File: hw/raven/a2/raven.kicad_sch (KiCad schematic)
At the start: 76 parts, among them J101 Pinhdr_01x02, J103 JTAG IN, J106 Pinhdr_01x02, J203 Pinhdr_01x03, SW2 SW_Push, U101 74LS148, U102 74AHC157, U103 SN74LVCH16245, U105 CY2308, U106 SN74LVCH16245, U108 ATF1508, U2 MC68060, U4 MC68150, X101 48Mhz (3.3V)

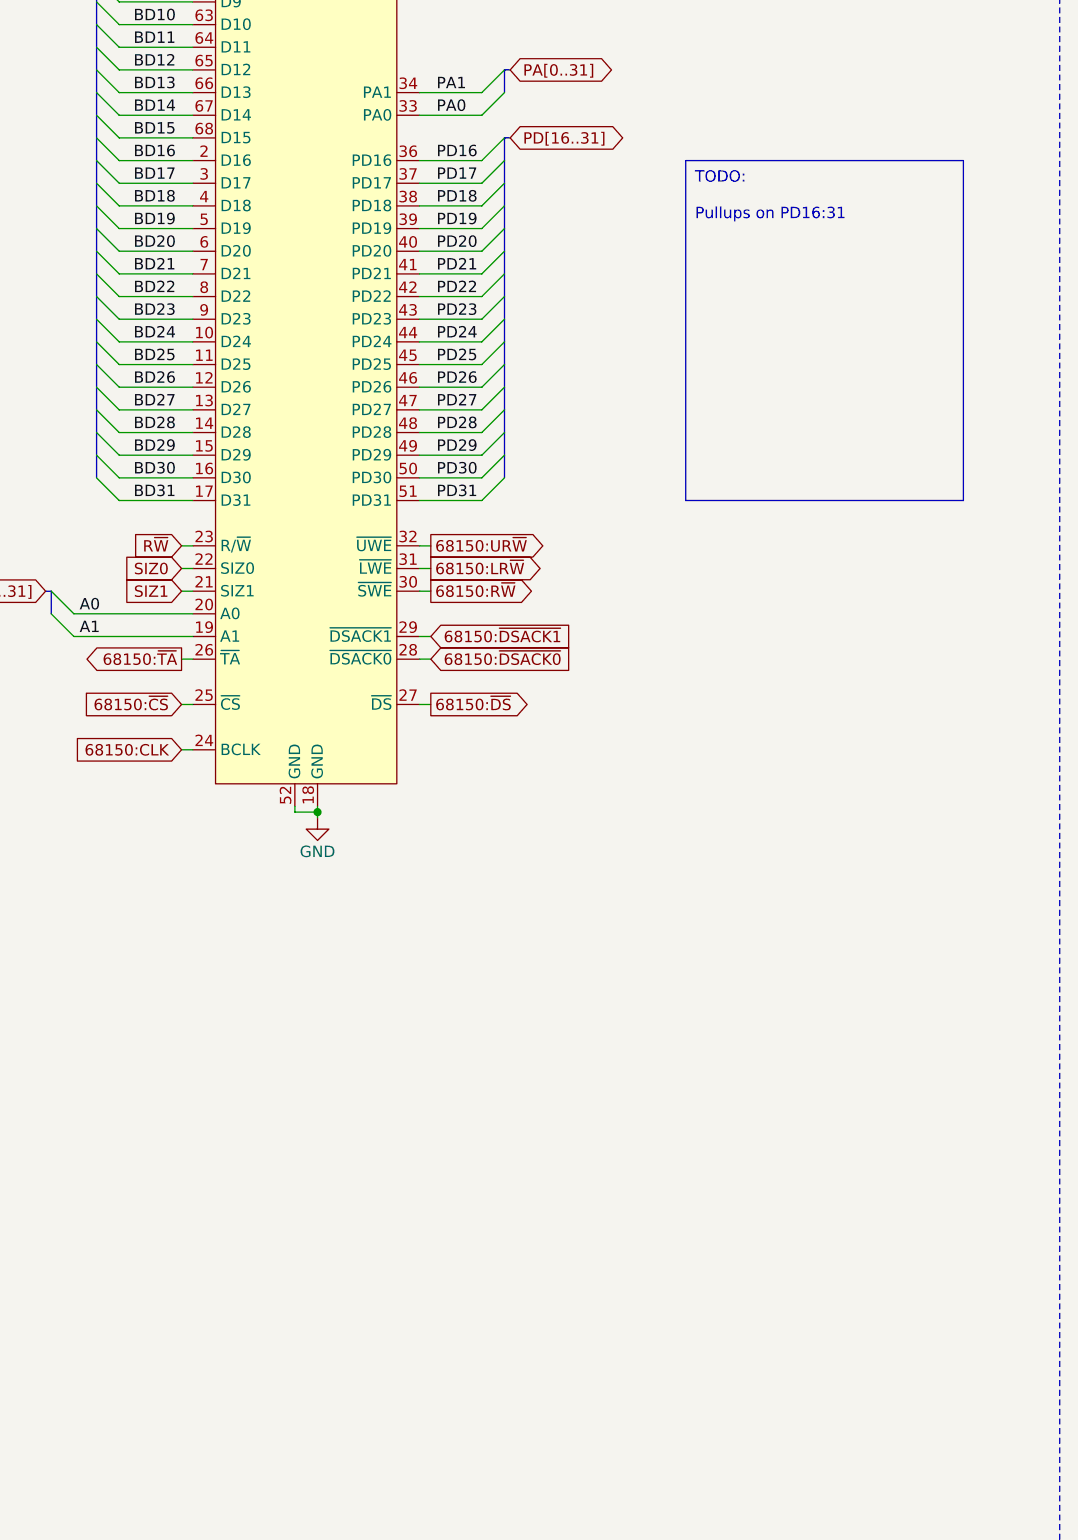
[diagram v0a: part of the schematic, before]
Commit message: Raven.A2: pullups on MC68150 databus
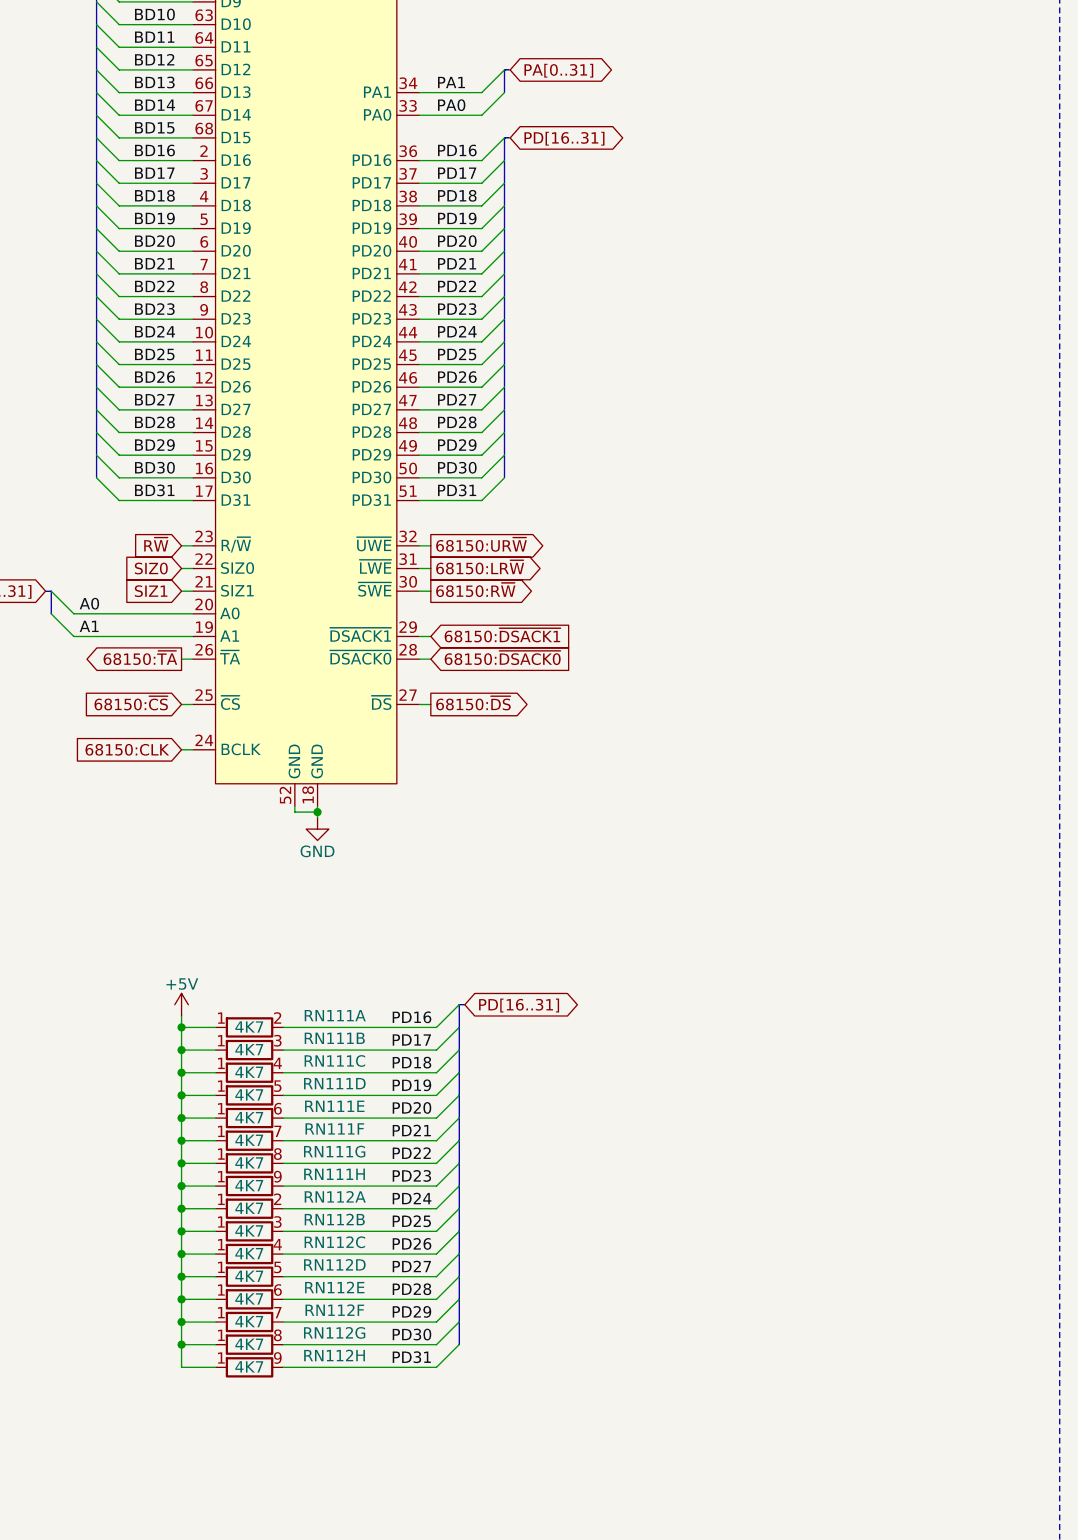
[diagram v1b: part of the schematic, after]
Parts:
- added RN111, RN112: 4K7, Resistor_THT:R_Array_SIP9, symbol Device:R_Network08_Split
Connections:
- net +5V: now also RN111.1 (R1), RN111.1 (R1), RN111.1 (R1), RN111.1 (R1), RN111.1 (R1), RN111.1 (R1), RN111.1 (R1), RN111.1 (R1), RN112.1 (R1), RN112.1 (R1), RN112.1 (R1), RN112.1 (R1), RN112.1 (R1), RN112.1 (R1), RN112.1 (R1), RN112.1 (R1)
- net PD16: now also RN111.2 (R1.2)
- net PD17: now also RN111.3 (R2.2)
- net PD18: now also RN111.4 (R3.2)
- net PD19: now also RN111.5 (R4.2)
- net PD20: now also RN111.6 (R5.2)
- net PD21: now also RN111.7 (R6.2)
- net PD22: now also RN111.8 (R7.2)
- net PD23: now also RN111.9 (R8.2)
- net PD24: now also RN112.2 (R1.2)
- net PD25: now also RN112.3 (R2.2)
- net PD26: now also RN112.4 (R3.2)
- net PD27: now also RN112.5 (R4.2)
- net PD28: now also RN112.6 (R5.2)
- net PD29: now also RN112.7 (R6.2)
- net PD30: now also RN112.8 (R7.2)
- net PD31: now also RN112.9 (R8.2)

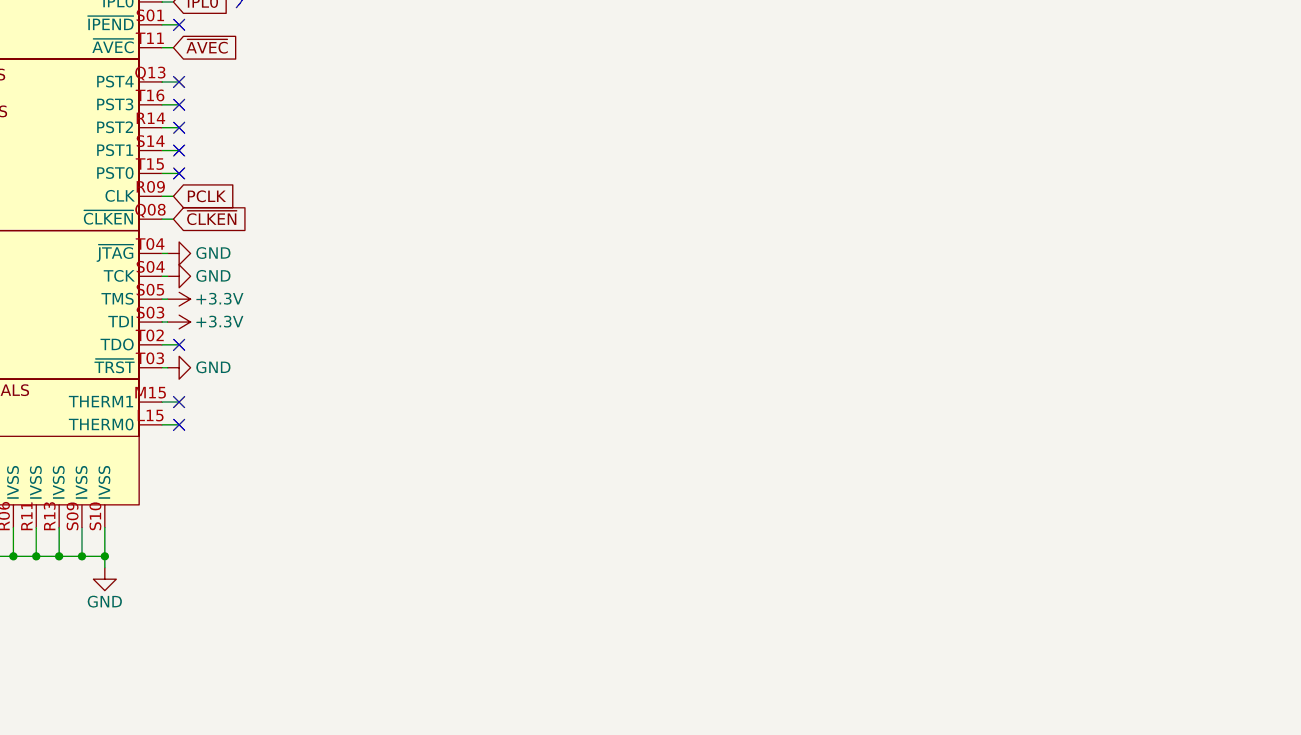
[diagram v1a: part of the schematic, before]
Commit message: rev.A2 updates
Added i2c DAC for reading cpu core temperature
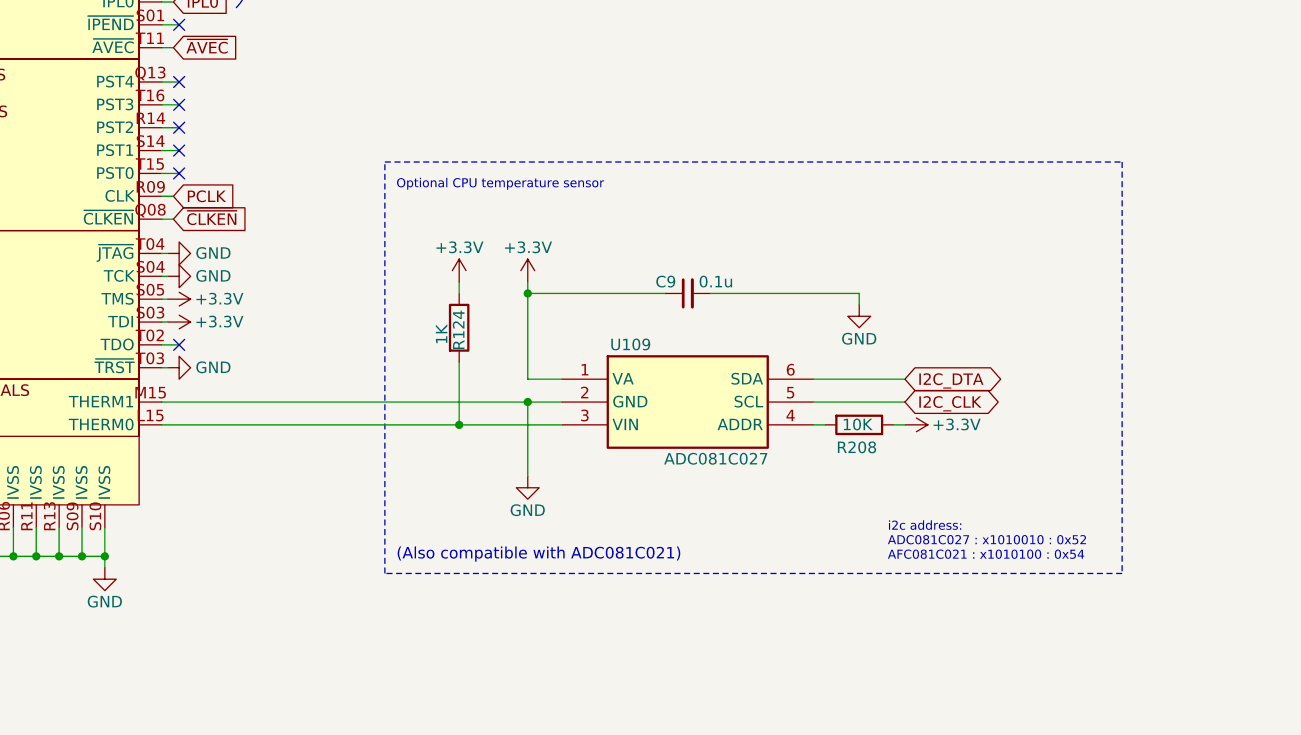
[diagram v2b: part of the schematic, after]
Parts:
- added C9: 0.1u, Capacitor_SMD:C_1206_3216Metric_Pad1.33x1.80mm_HandSolder, symbol 68k:c_100nf_smd1206
- added R124: 1K, Resistor_SMD:R_1206_3216Metric_Pad1.30x1.75mm_HandSolder, symbol Device:R
- added R208: 10K, Resistor_SMD:R_1206_3216Metric_Pad1.30x1.75mm_HandSolder, symbol Device:R
- added U109: ADC081C027, SOT95P280X110-6N, symbol 68k:ADC081C027CIMKX_NOPB
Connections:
- net +3.3V: now also C9.1, R124.1, R208.1, U109.1 (VA)
- net GND: now also U2.M15 (THERM1), C9.2, U109.2 (GND)
- net at U2.L15 (THERM0): now also R124.2, U109.3 (VIN)
- new net: R208.2, U109.4 (ADDR)
- new net I2C_CLK: U109.5 (SCL)
- new net I2C_DTA: U109.6 (SDA)
- no-connect marks 34 -> 32
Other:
- note added: "(Also compatible with ADC081C021)"
- note added: "Optional CPU temperature sensor"
- note added: "i2c address: ADC081C027 : x1010010 : 0x52 AFC081C021 : x1010100 : 0x54"

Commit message: Raven.A2 wip
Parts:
- removed C9: 0.1u, Capacitor_SMD:C_1206_3216Metric_Pad1.33x1.80mm_HandSolder, symbol 68k:c_100nf_smd1206
- removed J106: Pinhdr_01x02, Connector_PinHeader_2.54mm:PinHeader_1x02_P2.54mm_Vertical, symbol Connector_Generic:Conn_01x02
- removed R208: 10K, Resistor_SMD:R_1206_3216Metric_Pad1.30x1.75mm_HandSolder, symbol Device:R
- removed U109: ADC081C027, SOT95P280X110-6N, symbol 68k:ADC081C027CIMKX_NOPB
- renumbered C9 to C103, C10 to C104, C9 to C105, C9 to C106, C9 to C107, C514 to C108, C9 to C109, J203 to J102, J203 to J104, J203 to J105, SW2 to SW101, U4 to U104, U2 to U107
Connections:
- net PD17: now also RN112.2 (R1.2); no longer RN111.3 (R2.2)
- net PD18: now also RN111.3 (R2.2); no longer RN111.4 (R3.2)
- net PD19: now also RN112.3 (R2.2); no longer RN111.5 (R4.2)
- net PD20: now also RN111.4 (R3.2); no longer RN111.6 (R5.2)
- net PD21: now also RN112.4 (R3.2); no longer RN111.7 (R6.2)
- net PD22: now also RN111.5 (R4.2); no longer RN111.8 (R7.2)
- net PD23: now also RN112.5 (R4.2); no longer RN111.9 (R8.2)
- net PD24: now also RN111.6 (R5.2); no longer RN112.2 (R1.2)
- net PD25: now also RN112.6 (R5.2); no longer RN112.3 (R2.2)
- net PD26: now also RN111.7 (R6.2); no longer RN112.4 (R3.2)
- net PD27: now also RN112.7 (R6.2); no longer RN112.5 (R4.2)
- net PD28: now also RN111.8 (R7.2); no longer RN112.6 (R5.2)
- net PD29: now also RN112.8 (R7.2); no longer RN112.7 (R6.2)
- net PD30: now also RN111.9 (R8.2); no longer RN112.8 (R7.2)
- net ~{IRQ_MFP}: now also U101.2 (I5); no longer U101.3 (I6)
- net ~{IRQ_UART}: now also U101.3 (I6); no longer U101.2 (I5)
- net ~{ETH_CS}: now reaches U108.81 (GCLK3/IOH)
- net TEMP2: now reaches R124.2, U107.L15 (THERM0)
- no-connect marks 32 -> 33
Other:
- note added: "conflicting information"
- note added: "todo buffer cs"
- note removed: "(Also compatible with ADC081C021)"
- note removed: "Optional CPU temperature sensor"
- note removed: "i2c address: ADC081C027 : x1010010 : 0x52 AFC081C021 : x1010100 : 0x54"
- moved on the sheet: R124, RN111B, RN111C, RN111D, RN111E, RN111F, RN111G, RN111H, RN112A, RN112B, RN112C, RN112D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

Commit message: 68150:BUSCS signal separate from 68150:CS
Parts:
- removed R116: 1K, Resistor_SMD:R_1206_3216Metric_Pad1.30x1.75mm_HandSolder, symbol Device:R
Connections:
- net 68150:~{CS}: now also RN103.9 (R8.2); no longer U103.25 (~{OE2}), U103.48 (~{OE1}), U106.25 (~{OE2}), U106.48 (~{OE1})
- net 68150:~{BUSCS}: now reaches RN103.8 (R7.2)
- net 68150:~{BUSCS}: now also U103.25 (~{OE2}), U103.48 (~{OE1}), U106.25 (~{OE2}), U106.48 (~{OE1}), U108.73 (IOH)
- no-connect marks 33 -> 30
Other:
- note removed: "todo buffer cs"
- moved on the sheet: RN101A, RN101B, RN101C, RN101D, RN101E, RN101F, RN101G, RN101H, RN102D, RN102E, RN103D, RN103E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

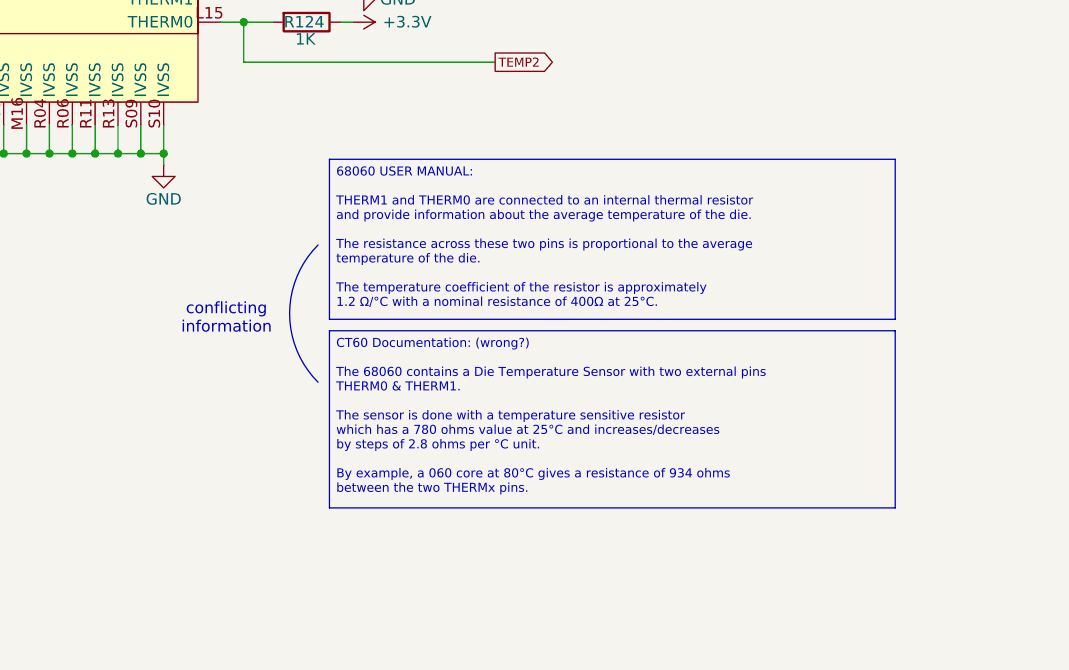
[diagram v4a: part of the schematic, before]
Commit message: A2 fan pwm+argb
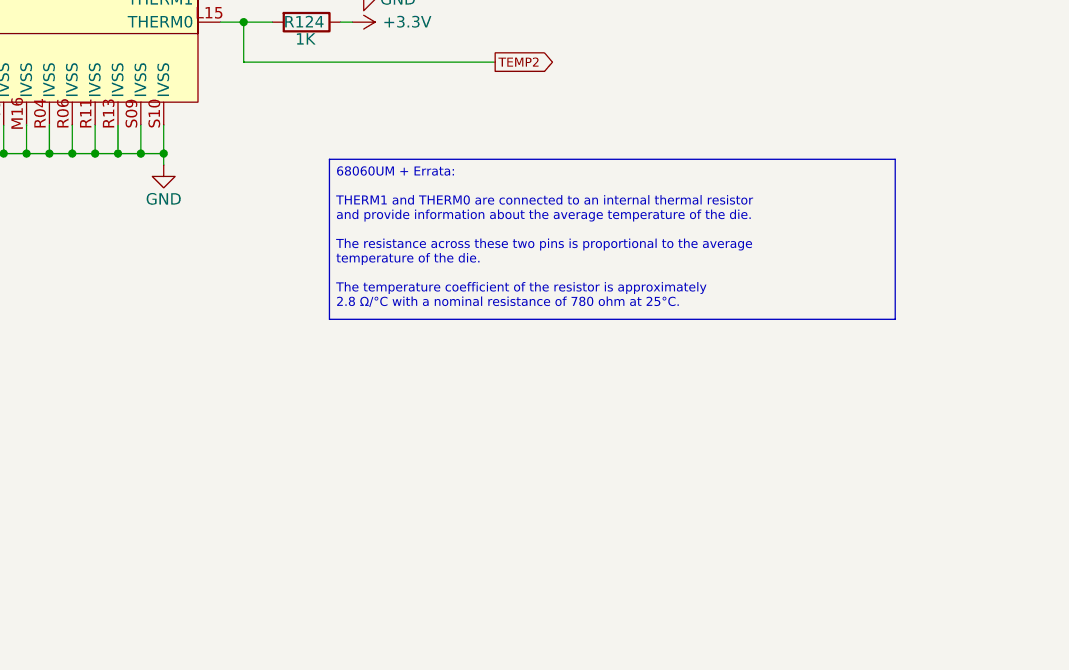
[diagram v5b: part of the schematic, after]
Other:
- note removed: "conflicting information"
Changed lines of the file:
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@@
-		)
-	)
-	(arc
-		(start 351.79 444.5)
-		(mid 348.6337 436.88)
-		(end 351.79 429.26)
-		(stroke
-			(width 0)
-			(type default)
-		)
-		(fill
-			(type none)
 		)
 	)
@@
 		)
 	)
-	(text "conflicting\ninformation"
-		(exclude_from_sim no)
-		(at 341.63 437.515 0)
-		(effects
-			(font
-				(size 1.27 1.27)
-			)
-		)
-	)
 	(text "Clock"
 		(exclude_from_sim no)
@@
 		)
 	)
-	(text_box "68060 USER MANUAL:\n\nTHERM1 and THERM0 are connected to an internal thermal resistor\nand provide information about the average temperature of the die.\n\nThe resistance across these two pins is proportional to the average\ntemperature of the die.\n\nThe temperature coefficient of the resistor is approximately\n1.2 Ω/°C with a nominal resistance of 400Ω at 25°C.\n"
+	(text_box "68060UM + Errata:\n\nTHERM1 and THERM0 are connected to an internal thermal resistor\nand provide information about the average temperature of the die.\n\nThe resistance across these two pins is proportional to the average\ntemperature of the die.\n\nThe temperature coefficient of the resistor is approximately\n2.8 Ω/°C with a nominal resistance of 780 ohm at 25°C.\n"
 		(exclude_from_sim no)
 		(at 353.06 419.735 0)
@@
 			)
 			(justify left top)
-		)
-	)
-	(text_box "CT60 Documentation: (wrong?)\n\nThe 68060 contains a Die Temperature Sensor with two external pins\nTHERM0 & THERM1.\n\nThe sensor is done with a temperature sensitive resistor\nwhich has a 780 ohms value at 25°C and increases/decreases\nby steps of 2.8 ohms per °C unit.\n\nBy example, a 060 core at 80°C gives a resistance of 934 ohms\nbetween the two THERMx pins.\n"
-		(exclude_from_sim no)
-		(at 353.06 438.785 0)
-		(size 62.865 19.685)
-		(margins 0.75 0.75 0.75 0.75)
-		(stroke
-			(width 0)
-			(type solid)
-		)
-		(fill
-			(type none)
-		)
-		(effects
-			(font
-				(size 1 1)
-			)
-			(justify left top)

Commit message: a2 wip
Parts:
- added R121, R122: 1K, Resistor_SMD:R_1206_3216Metric_Pad1.30x1.75mm_HandSolder, symbol Device:R
- renumbered C121 to C112, C122 to C113, C123 to C114, C124 to C115, C125 to C116, C126 to C117, C127 to C118, C128 to C119, C112 to C120, C113 to C121, C114 to C122, C115 to C123, C116 to C124, C117 to C125, C118 to C126, C119 to C127, C120 to C128, R117 to R116, R118 to R117, R119 to R118, R120 to R119, R124 to R120, R121 to R123, R122 to R124, RN111 to RN101, RN112 to RN102, RN104 to RN103, RN101 to RN104, RN102 to RN106, RN106 to RN107, RN107 to RN108, RN103 to RN109, RN108 to RN110, RN109 to RN111, RN110 to RN112
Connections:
- net +3.3V: now also R121.1, R122.1
- net A0: now also R121.2
- net A1: now also R122.2
- net A5: no longer U108.34 (IOD)
- net A6: now also U108.34 (IOD)
- net R~{W}: now also RN104.5 (R4.2); no longer RN104.9 (R8.2)
- net ~{BGR}: now also RN104.9 (R8.2); no longer RN104.8 (R7.2)
- net ~{CLA}: now also RN104.8 (R7.2); no longer RN104.7 (R6.2)
- net ~{SAS}: now also RN104.6 (R5.2); no longer RN104.5 (R4.2)
- net ~{SNOOP}: now also RN104.7 (R6.2); no longer RN104.6 (R5.2)
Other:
- note added: "Bus logic"
- note added: "CPU"
- moved on the sheet: C112, C113, C114, C115, C116, C117, C118, C119, C120, C121, C122, C123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
